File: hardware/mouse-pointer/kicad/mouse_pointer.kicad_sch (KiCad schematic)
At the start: 24 parts, among them J1 Conn_PinHeader, J2 Conn_FPC, U1 PMW3610, U2 TLV74318PDBVR

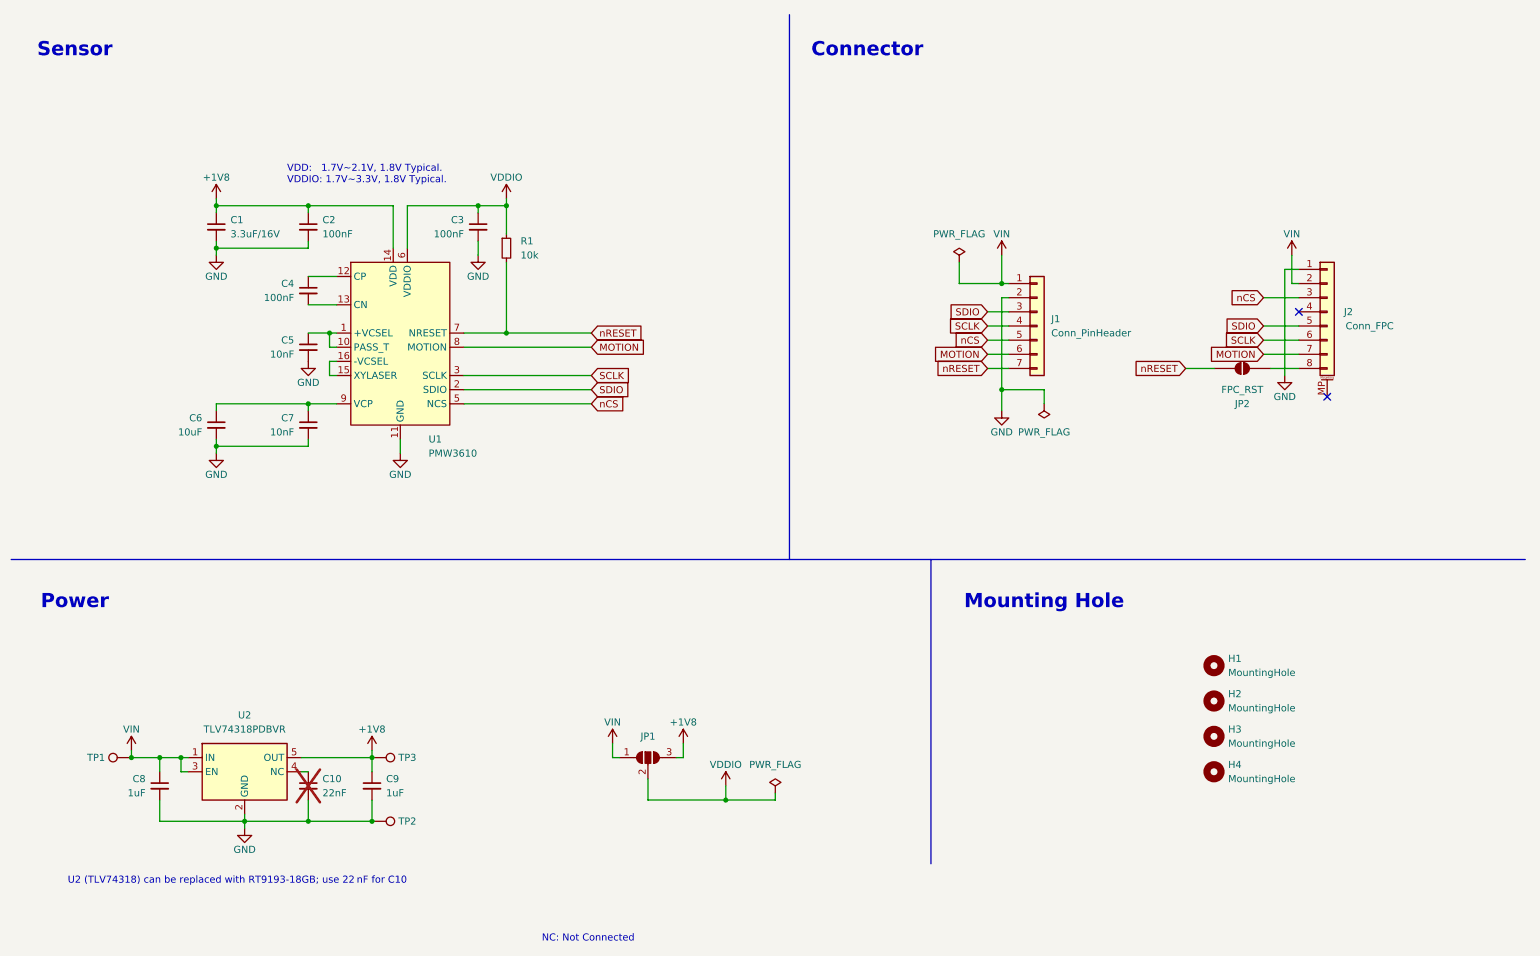
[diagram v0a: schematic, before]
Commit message: feat: add RJ45 mouse pointer board interface
- Add the ClickTapToe 8P8C/RJ45 pinout to the PMW3610 mouse pointer board.
  - Add reset and VDDIO configuration links, optional nCS pull-up, and MOTION series resistor.
  - Extend the board layout for the RJ45 connector and added mounting holes.
  - Document revised mouse pointer cabling, twisted-pair grouping, and input hub wiring contract.
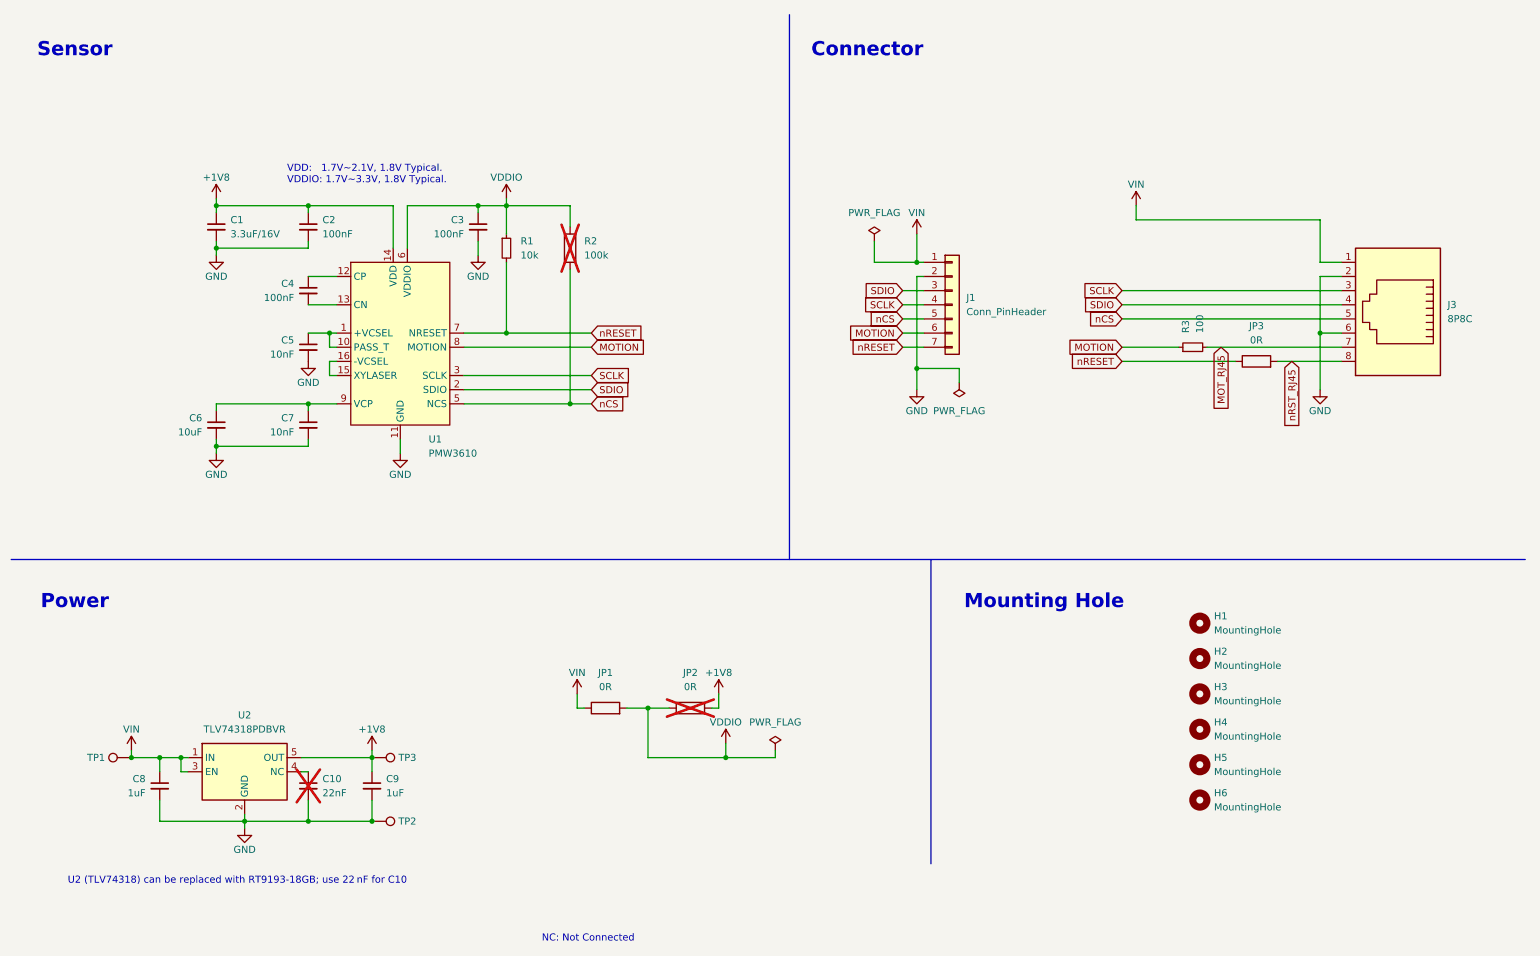
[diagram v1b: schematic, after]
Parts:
- removed J2: Conn_FPC, mouse_pointer:FPC_8P_0.5mm_AFC01-S08FCA-00, symbol Connector_Generic_MountingPin:Conn_01x08_MountingPin
- removed JP1: SolderJumper_3_Open, Jumper:SolderJumper-3_P1.3mm_Open_RoundedPad1.0x1.5mm_NumberLabels, symbol Jumper:SolderJumper_3_Open
- removed JP2: FPC_RST, Jumper:SolderJumper-2_P1.3mm_Open_RoundedPad1.0x1.5mm, symbol Jumper:SolderJumper_2_Open
- added H5, H6: MountingHole, MountingHole:MountingHole_3.2mm_M3_ISO14580, symbol Mechanical:MountingHole
- added J3: 8P8C, Connector_RJ:RJ45_Amphenol_54602-x08_Horizontal, symbol Connector:8P8C
- added JP1, JP2, JP3: 0R, Resistor_SMD:R_0603_1608Metric, symbol Device:R
- added R2: 100k, Resistor_SMD:R_0603_1608Metric, symbol Device:R
- added R3: 100, Resistor_SMD:R_0603_1608Metric, symbol Device:R_Small
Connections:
- net +1V8: now also JP2.2
- net GND: now also J3.2, J3.6
- net MOTION: now also R3.1
- net SCLK: now also J3.3
- net SDIO: now also J3.4
- net VDDIO: now also JP1.2, JP2.1, R2.1
- net VIN: now also J3.1, JP1.1
- net nCS: now also J3.5, R2.2
- net nRESET: now also JP3.1
- new net MOT_RJ45: J3.7, R3.2
- new net nRST_RJ45: J3.8, JP3.2
- no-connect marks 2 -> 0
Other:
- company: SideraKB -> Mazzorella
- title: PMW3610 PCB -> Mouse Pointer
- moved on the sheet: H1, H2, H3, H4, J1

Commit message: feat: add ESD protection to mouse pointer and update board fields
- Add ESD protection, logo artwork, and final board manufacturing fields.
  - Include generated fabrication outputs for direct ordering.
  - Document hand-installed RJ45, optional tester header, and board configuration.
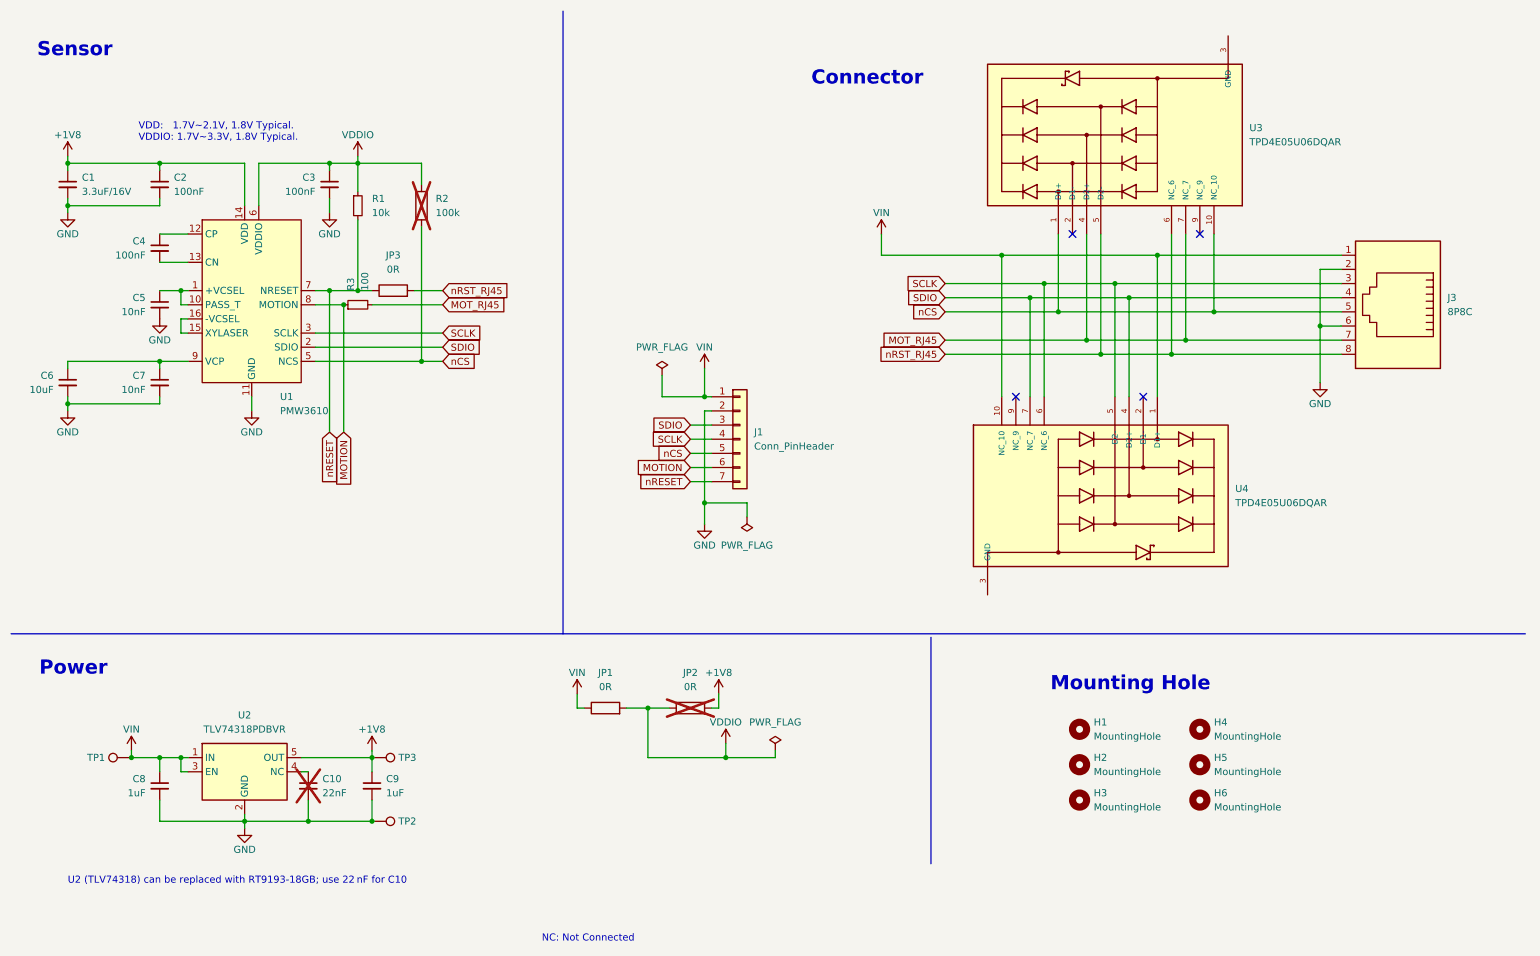
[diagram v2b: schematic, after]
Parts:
- added U3, U4: TPD4E05U06DQAR, mouse_pointer:IC_TPD4E05U06DQAR, symbol TPD:TPD4E05U06DQAR
- JP1, JP2, JP3: JLCPCB Part # (none) -> C21189; MFR. Part # (none) -> 0603WAF0000T5E
- R2: JLCPCB Part # (none) -> C25803; MFR. Part # (none) -> 0603WAF1003T5E
- R3: JLCPCB Part # C25804 -> C22775; MFR. Part # 0603WAF1002T5E -> 0603WAF1000T5E
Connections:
- net GND: now also U3.3 (GND), U3.8 (GND), U4.3 (GND), U4.8 (GND)
- net MOT_RJ45: now also U3.4 (D2+), U3.7 (NC_7)
- net SCLK: now also U4.5 (D2-), U4.6 (NC_6)
- net SDIO: now also U4.4 (D2+), U4.7 (NC_7)
- net VIN: now also U4.1 (D1+), U4.10 (NC_10)
- net nCS: now also U3.1 (D1+), U3.10 (NC_10)
- net nRST_RJ45: now also U3.5 (D2-), U3.6 (NC_6)
- no-connect marks 0 -> 4
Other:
- moved on the sheet: C1, C2, C3, C4, C5, C6, C7, H1, H2, H3, J1, J3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

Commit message: feat: updated board for JLC constraints, add 3D models, add silkscreen logos, correct production outputs
- Add Cal Poly and EMPOWER silkscreen artwork and generated KiCad footprints.
  - Add PMW3610 and RJ45 model assets for board review.
  - Update JLC board constraints and clean up resulting DRC issues.
  - Update ESD placement rotation fields for JLC assembly output.
  - Exclude optional headers, RJ45s, DNP parts, test points, and holes from assembly files.
  - Regenerate mouse pointer production BOM, CPL, netlist, and fabrication archive.
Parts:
- C1: Manufacturer (none) -> CCTC
- C10, C6, C8, C9: Manufacturer (none) -> Samsung Electro-Mechanics
- C2, C3, C4: Manufacturer (none) -> YAGEO
- C5, C7: Manufacturer (none) -> FH (Guangdong Fenghua Advanced Tech)
- J1: now not fitted; now left out of the parts list
- J2: renamed from J3; value 8P8C -> 54602-908LF; footprint Connector_RJ:RJ45_Amphenol_54602-x08_Horizontal -> mouse_pointer:RJ45_Amphenol_54602-x08_Horizontal; Digi-Key MFR. Part # (none) -> 54602-908LF; Digi-Key Part # (none) -> 609-1046-ND; MFR. Part # (none) -> 54602-908LF; Manufacturer (none) -> Amphenol ICC (FCI); now left out of the parts list
- JP1, JP2, JP3, R1, R2, R3: Manufacturer (none) -> UNI-ROYAL
- U1: Manufacturer (none) -> PixArt Imaging
- U2: Manufacturer (none) -> Texas Instruments
- U3, U4: FT Rotation Offset (none) -> 270
